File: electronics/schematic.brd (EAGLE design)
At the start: 20.3 x 15.9 mm, 22 parts, among them Q2 NX3008NBK

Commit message: new board design
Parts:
- added R5: (no value), resistor:M0805
- moved SYNC1 104.8 mm to (30.5, 35.6)
- moved SYNC0 99.8 mm to (30.5, 33.0)
- moved Q2 89.6 mm to (26.7, 41.9)
- moved R4 41.8 mm to (-15.2, 27.9)
- moved R3 33.0 mm to (-34.3, 21.6)
- moved VBAT+ 31.5 mm to (30.5, 45.7)
- moved C1 31.4 mm to (30.5, 41.9)
- moved R2 27.1 mm to (-29.2, 21.6)
- moved VBAT- 25.9 mm to (30.5, 38.1)
- moved LED1 25.1 mm to (-25.4, 14.0)
- moved LED2 23.9 mm to (-30.5, 14.0)
- moved LED3 22.8 mm to (-35.6, 14.0)
- moved GND 22.4 mm to (10.2, 35.6)
- moved RST 22.4 mm to (10.2, 33.0)
- moved TEST 22.4 mm to (10.2, 40.6)
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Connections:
- net LED: no longer U$1.13
- net RST: now also R5.1, U$1.7
- net VCC: now also R5.2; no longer U$1.7
- net XIN: now also U$2.P$2; no longer U$2.P$1
- net XOUT: now also U$2.P$1; no longer U$2.P$2
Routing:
- net P2.0: track 0.00 -> 12.6 mm, vias 0 -> 2
- net VCC: track 27.5 -> 38.6 mm, vias 2 -> 4
- net GND: track 44.4 -> 36.4 mm, vias 2 -> 0
- net LED: track 5.89 -> 0.00 mm
- net RST: track 10.3 -> 15.6 mm, vias 0 -> 2
- net XOUT: track 11.5 -> 16.5 mm
- net XIN: track 8.29 -> 12.5 mm
- net TXD: track 10.2 -> 10.7 mm
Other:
- board size 20.3 x 15.9 mm -> 100 x 80 mm

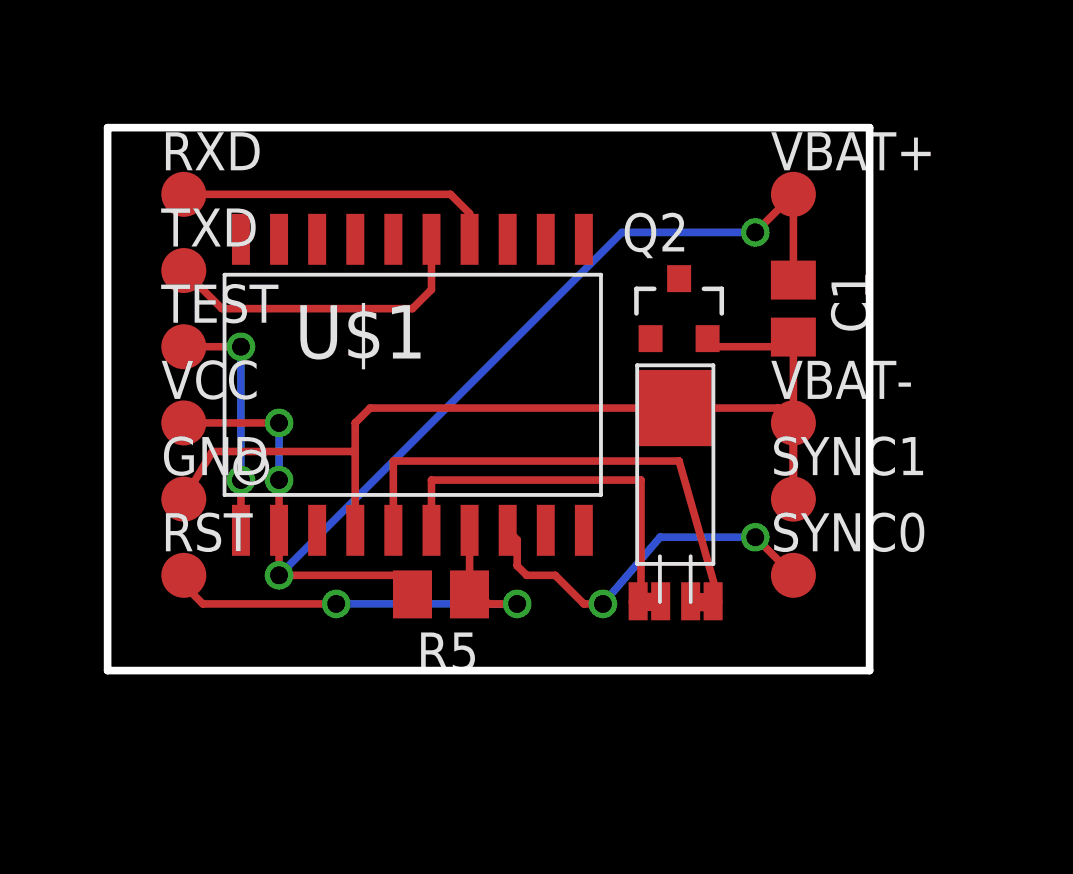
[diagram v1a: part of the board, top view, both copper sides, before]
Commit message: Moved cap closer to micro
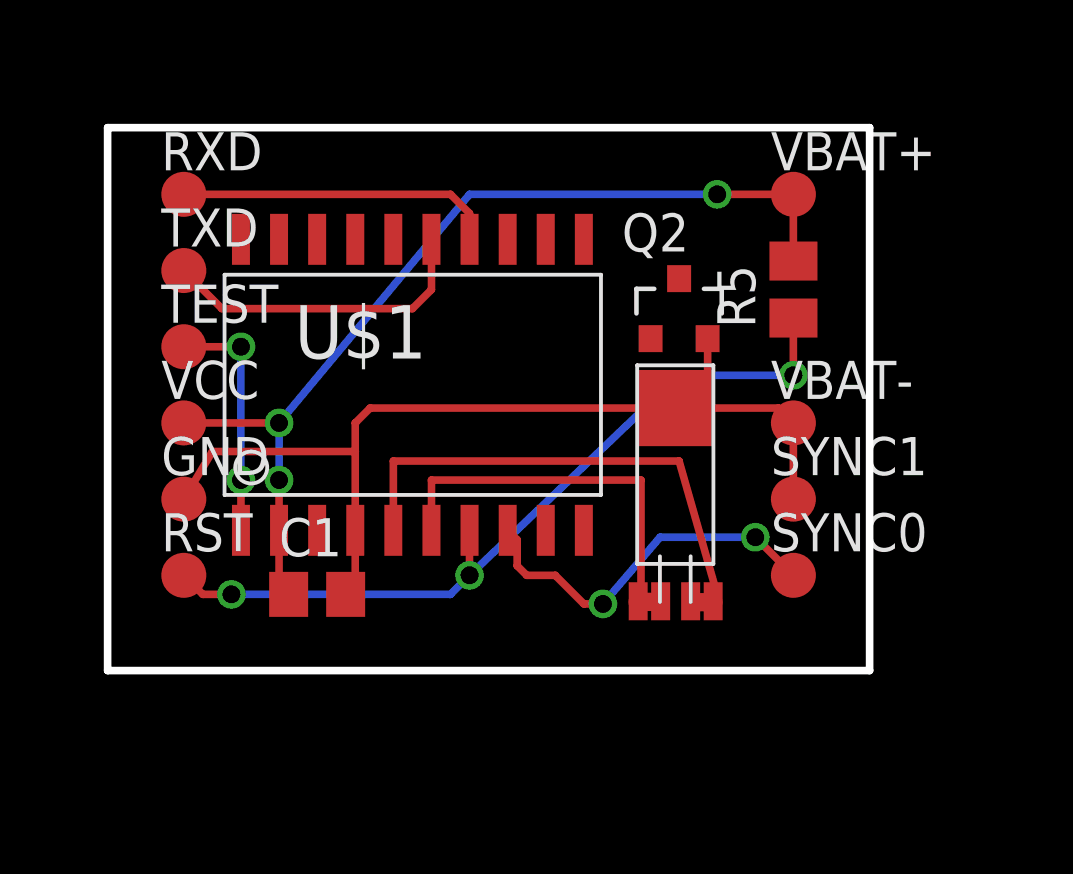
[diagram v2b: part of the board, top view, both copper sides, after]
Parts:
- moved C1 18.5 mm to (14.6, 32.4), turned to 0 degrees
- moved R5 15.5 mm to (30.5, 42.5), turned to 90 degrees
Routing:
- net RST: track 15.6 -> 26.9 mm, vias 2 -> 3
- net VCC: track 38.6 -> 32.0 mm, vias 4 -> 3
- net GND: track 36.4 -> 32.8 mm
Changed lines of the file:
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@@
 </autorouter>
 <elements>
-<element name="C1" library="resistor" package="C0805" value="" x="30.48" y="41.91" rot="R270"/>
+<element name="C1" library="resistor" package="C0805" value="" x="14.605" y="32.385"/>
 <element name="GND" library="testpad" package="TP15R" value="TPTP15R" x="10.16" y="35.56">
 <attribute name="TP_SIGNAL_NAME" value="" x="10.16" y="35.56" size="1.778" layer="27" display="off"/>
@@
 <attribute name="TP_SIGNAL_NAME" value="" x="10.16" y="38.1" size="1.778" layer="27" display="off"/>
 </element>
-<element name="R5" library="resistor" package="M0805" value="" x="18.7325" y="32.385" rot="R180"/>
+<element name="R5" library="resistor" package="M0805" value="" x="30.48" y="42.545" rot="R90"/>
 </elements>
 <signals>
@@
 <contactref element="U$1" pad="7"/>
 <contactref element="R5" pad="1"/>
-<wire x1="19.6825" y1="32.385" x2="19.685" y2="32.3875" width="0.254" layer="1"/>
-<wire x1="19.685" y1="32.3875" x2="19.685" y2="34.52" width="0.254" layer="1"/>
-<via x="21.2725" y="32.0675" extent="1-16" drill="0.6" shape="square"/>
-<via x="15.24" y="32.0675" extent="1-16" drill="0.6" shape="square"/>
-<wire x1="15.24" y1="32.0675" x2="10.795" y2="32.0675" width="0.254" layer="1"/>
-<wire x1="10.795" y1="32.0675" x2="10.16" y2="32.7025" width="0.254" layer="1"/>
-<wire x1="10.16" y1="32.7025" x2="10.16" y2="33.02" width="0.254" layer="1"/>
-<wire x1="15.24" y1="32.0675" x2="21.2725" y2="32.0675" width="0.254" layer="16"/>
-<wire x1="21.2725" y1="32.0675" x2="20.32" y2="32.0675" width="0.254" layer="1"/>
-<wire x1="20.32" y1="32.0675" x2="20.0025" y2="32.385" width="0.254" layer="1"/>
-<wire x1="20.0025" y1="32.385" x2="19.6825" y2="32.385" width="0.254" layer="1"/>
+<wire x1="19.685" y1="34.52" x2="19.685" y2="33.02" width="0.254" layer="1"/>
+<via x="19.685" y="33.02" extent="1-16" drill="0.6" shape="square"/>
+<wire x1="19.685" y1="33.02" x2="26.67" y2="39.6875" width="0.254" layer="16"/>
+<wire x1="26.67" y1="39.6875" x2="30.48" y2="39.6875" width="0.254" layer="16"/>
+<via x="30.48" y="39.6875" extent="1-16" drill="0.6" shape="square"/>
+<wire x1="30.48" y1="39.6875" x2="30.48" y2="41.595" width="0.254" layer="1"/>
+<wire x1="10.16" y1="33.02" x2="10.795" y2="32.385" width="0.254" layer="1"/>
+<wire x1="10.795" y1="32.385" x2="11.7475" y2="32.385" width="0.254" layer="1"/>
+<via x="11.7475" y="32.385" extent="1-16" drill="0.6" shape="square"/>
+<wire x1="11.7475" y1="32.385" x2="19.05" y2="32.385" width="0.254" layer="16"/>
+<wire x1="19.05" y1="32.385" x2="19.685" y2="33.02" width="0.254" layer="16"/>
 </signal>
 <signal name="VCC">
@@
 <via x="13.335" y="38.1" extent="1-16" drill="0.6" shape="square"/>
 <wire x1="13.335" y1="38.1" x2="10.16" y2="38.1" width="0.254" layer="1"/>
-<wire x1="30.48" y1="42.86" x2="30.48" y2="45.72" width="0.254" layer="1"/>
-<wire x1="13.335" y1="34.52" x2="13.335" y2="33.02" width="0.254" layer="1"/>
-<via x="13.335" y="33.02" extent="1-16" drill="0.6" shape="square"/>
-<wire x1="13.335" y1="33.02" x2="24.765" y2="44.45" width="0.254" layer="16"/>
-<wire x1="24.765" y1="44.45" x2="29.21" y2="44.45" width="0.254" layer="16"/>
-<via x="29.21" y="44.45" extent="1-16" drill="0.6" shape="square"/>
-<wire x1="29.21" y1="44.45" x2="30.48" y2="45.72" width="0.254" layer="1"/>
+<wire x1="30.48" y1="43.495" x2="30.48" y2="44.45" width="0" layer="19" extent="1-16"/>
+<wire x1="30.48" y1="43.495" x2="30.48" y2="45.72" width="0.254" layer="1"/>
+<wire x1="13.335" y1="38.1" x2="19.685" y2="45.72" width="0.254" layer="16"/>
+<wire x1="19.685" y1="45.72" x2="27.94" y2="45.72" width="0.254" layer="16"/>
+<via x="27.94" y="45.72" extent="1-16" drill="0.6" shape="square"/>
 <wire x1="-13.97" y1="21.81" x2="10.16" y2="38.1" width="0" layer="19" extent="1-1"/>
 <wire x1="-25.4" y1="12.92" x2="-13.97" y2="21.81" width="0" layer="19" extent="1-1"/>
 <wire x1="-30.48" y1="12.92" x2="-25.4" y2="12.92" width="0" layer="19" extent="1-1"/>
 <wire x1="-35.56" y1="12.92" x2="-30.48" y2="12.92" width="0" layer="19" extent="1-1"/>
-<wire x1="13.335" y1="33.02" x2="17.78" y2="33.02" width="0.254" layer="1"/>
-<wire x1="17.78" y1="33.02" x2="17.7825" y2="33.0175" width="0.254" layer="1"/>
-<wire x1="17.7825" y1="33.0175" x2="17.7825" y2="32.385" width="0.254" layer="1"/>
+<wire x1="13.655" y1="32.385" x2="13.335" y2="32.705" width="0.254" layer="1"/>
+<wire x1="13.335" y1="32.705" x2="13.335" y2="34.52" width="0.254" layer="1"/>
+<wire x1="30.48" y1="45.72" x2="30.48" y2="45.72" width="0" layer="19" extent="1-16"/>
+<wire x1="27.94" y1="45.72" x2="30.48" y2="45.72" width="0.254" layer="1"/>
 </signal>
 <signal name="TXD">
@@
 <wire x1="30.48" y1="38.1" x2="29.984" y2="38.596" width="0.254" layer="1"/>
 <wire x1="29.984" y1="38.596" x2="26.543" y2="38.596" width="0.254" layer="1"/>
-<wire x1="30.48" y1="35.56" x2="30.48" y2="40.96" width="0.254" layer="1"/>
 <wire x1="15.875" y1="34.52" x2="15.875" y2="37.1475" width="0.254" layer="1"/>
 <wire x1="15.875" y1="37.1475" x2="15.875" y2="38.1" width="0.254" layer="1"/>
@@
 <wire x1="10.16" y1="35.56" x2="11.1125" y2="37.1475" width="0.254" layer="1"/>
 <wire x1="11.1125" y1="37.1475" x2="15.875" y2="37.1475" width="0.254" layer="1"/>
-<wire x1="30.48" y1="40.96" x2="30.16" y2="40.64" width="0.254" layer="1"/>
-<wire x1="30.16" y1="40.64" x2="27.6225" y2="40.64" width="0.254" layer="1"/>
-<wire x1="27.6225" y1="40.64" x2="27.62" y2="40.6425" width="0.254" layer="1"/>
-<wire x1="27.62" y1="40.6425" x2="27.62" y2="40.91" width="0.254" layer="1"/>
+<wire x1="15.555" y1="32.385" x2="15.875" y2="32.705" width="0.254" layer="1"/>
+<wire x1="15.875" y1="32.705" x2="15.875" y2="34.52" width="0.254" layer="1"/>
+<wire x1="26.543" y1="38.596" x2="27.62" y2="39.673" width="0.254" layer="1"/>
+<wire x1="27.62" y1="39.673" x2="27.62" y2="40.91" width="0.254" layer="1"/>
 </signal>
 <signal name="N$4">
